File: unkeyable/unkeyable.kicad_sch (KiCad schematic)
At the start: 12 parts, among them SW1 1, SW10 F, SW11 J, SW12 K, SW2 C, SW3 3, SW4 Q, SW5 W, SW6 E, SW7 A, SW8 S, SW9 D

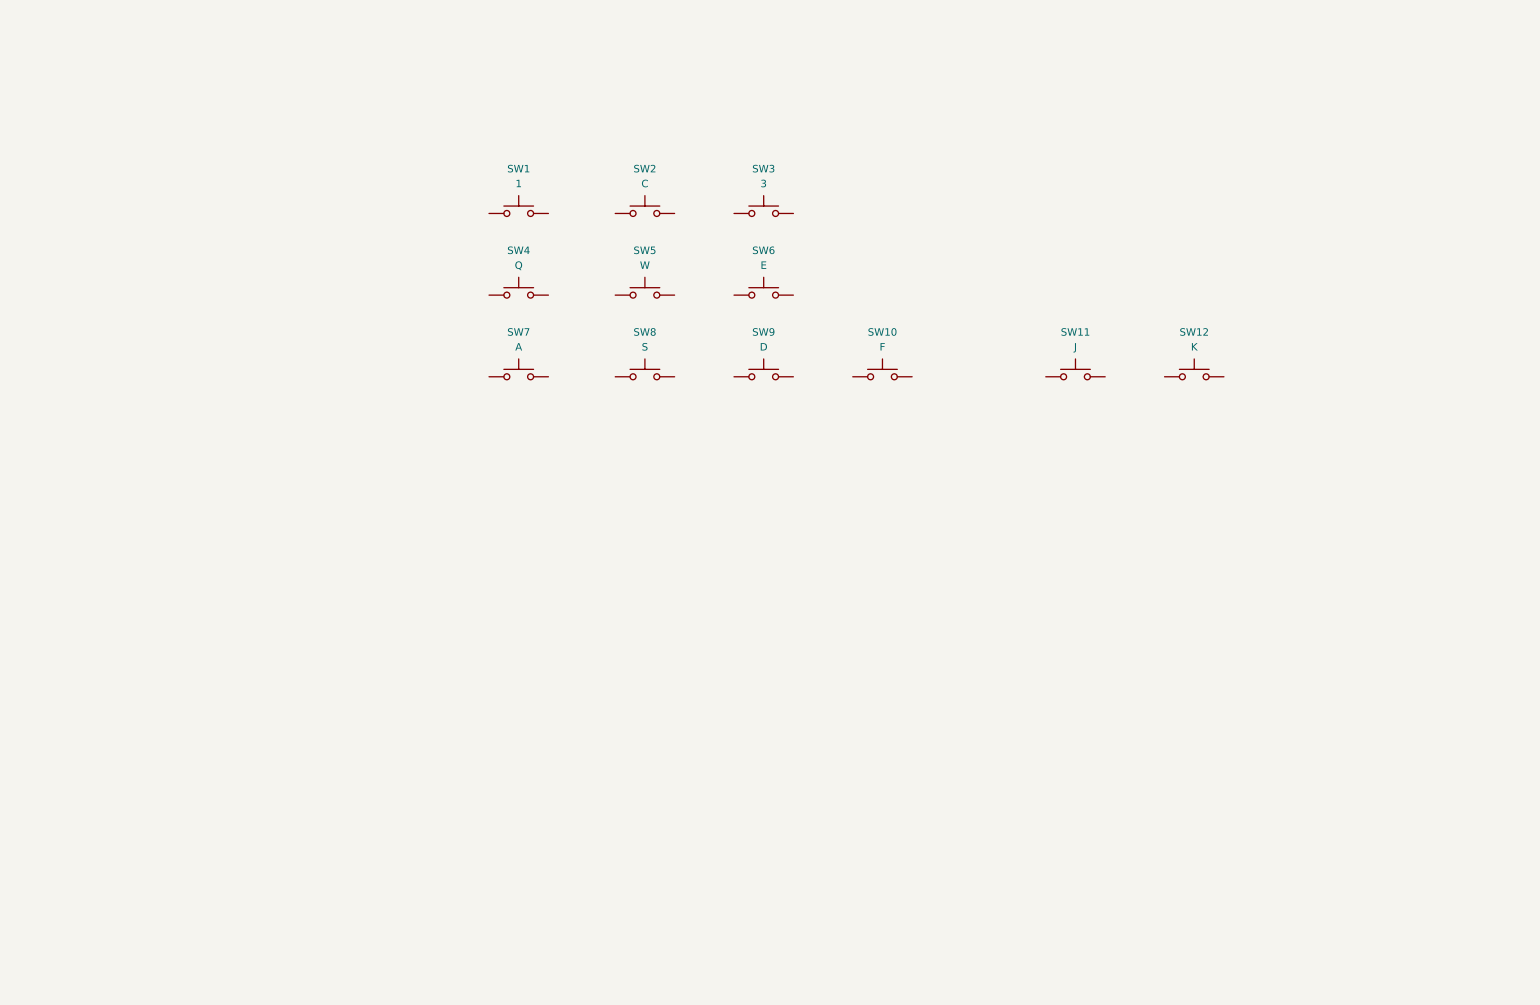
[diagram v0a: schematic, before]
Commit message: Adding RP2040 minimal viable schematic
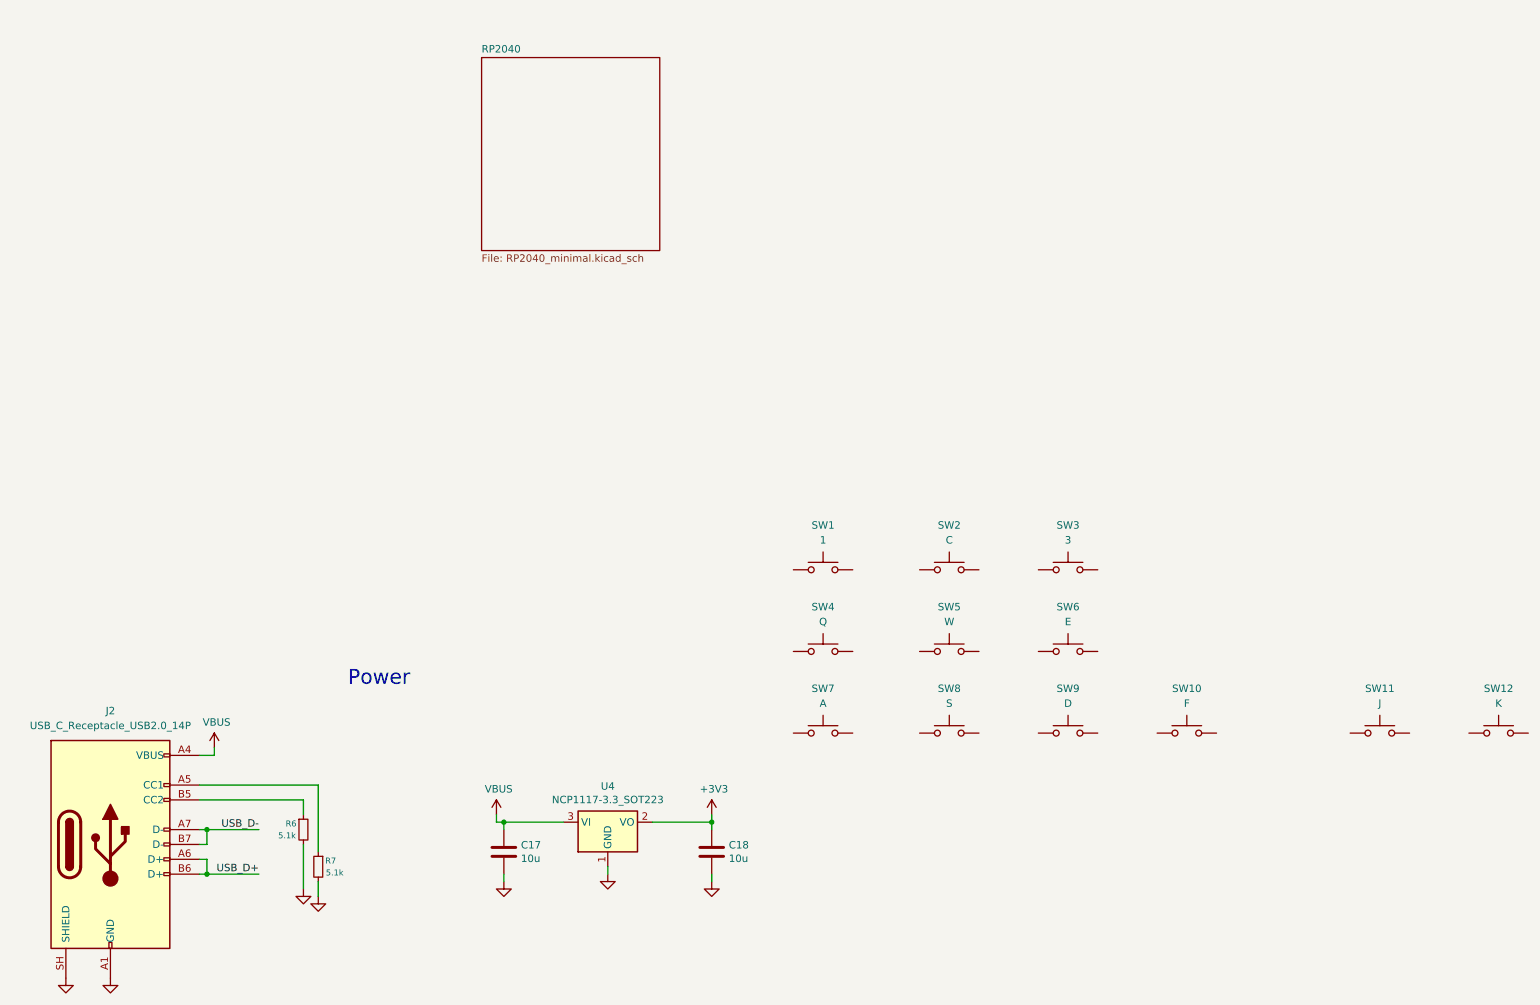
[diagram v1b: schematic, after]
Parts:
- added C17, C18: 10u, Capacitor_SMD:C_0805_2012Metric, symbol Device:C
- added J2: USB_C_Receptacle_USB2.0_14P, symbol Connector:USB_C_Receptacle_USB2.0_14P
- added R6, R7: 5.1k, symbol Device:R_Small
- added U4: NCP1117-3.3_SOT223, Package_TO_SOT_SMD:SOT-223-3_TabPin2, symbol Regulator_Linear:NCP1117-3.3_SOT223
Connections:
- new net: J2.A5 (CC1), R7.1
- new net: J2.B5 (CC2), R6.1
- new net +3V3: C18.1, U4.2 (VO)
- new net GND: C17.2, C18.2, J2.A1 (GND), J2.A12 (GND), J2.B1 (GND), J2.B12 (GND), J2.SH (SHIELD), R6.2, R7.2, U4.1 (GND)
- new net USB_D+: J2.A6 (D+), J2.B6 (D+)
- new net USB_D-: J2.A7 (D-), J2.B7 (D-)
- new net VBUS: C17.1, J2.A4 (VBUS), J2.A9 (VBUS), J2.B4 (VBUS), J2.B9 (VBUS), U4.3 (VI)
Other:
- added sheet RP2040 (RP2040_minimal.kicad_sch)
- note added: "Power"
- moved on the sheet: SW1, SW10, SW11, SW12, SW2, SW3, SW4, SW5, SW6, SW7, SW8, SW9

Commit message: working on Schematics
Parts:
- removed SW1: 1, Button_Switch_Keyboard:SW_Cherry_MX_1.00u_PCB, symbol Switch:SW_Push
- removed SW10: F, Button_Switch_Keyboard:SW_Cherry_MX_1.00u_PCB, symbol Switch:SW_Push
- removed SW11: J, Button_Switch_Keyboard:SW_Cherry_MX_1.00u_PCB, symbol Switch:SW_Push
- removed SW12: K, Button_Switch_Keyboard:SW_Cherry_MX_1.00u_PCB, symbol Switch:SW_Push
- removed SW2: C, Button_Switch_Keyboard:SW_Cherry_MX_1.00u_PCB, symbol Switch:SW_Push
- removed SW3: 3, Button_Switch_Keyboard:SW_Cherry_MX_1.00u_PCB, symbol Switch:SW_Push
- removed SW4: Q, Button_Switch_Keyboard:SW_Cherry_MX_1.00u_PCB, symbol Switch:SW_Push
- removed SW5: W, Button_Switch_Keyboard:SW_Cherry_MX_1.00u_PCB, symbol Switch:SW_Push
- removed SW6: E, Button_Switch_Keyboard:SW_Cherry_MX_1.00u_PCB, symbol Switch:SW_Push
- removed SW7: A, Button_Switch_Keyboard:SW_Cherry_MX_1.00u_PCB, symbol Switch:SW_Push
- removed SW8: S, Button_Switch_Keyboard:SW_Cherry_MX_1.00u_PCB, symbol Switch:SW_Push
- removed SW9: D, Button_Switch_Keyboard:SW_Cherry_MX_1.00u_PCB, symbol Switch:SW_Push
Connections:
- net VBUS renamed +5V
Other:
- added sheet Switch_Matrix (Switch_Matrix.kicad_sch)
- sheet RP2040 ports: added GPIO0, GPIO1, GPIO10, GPIO11, GPIO12, GPIO13, GPIO14, GPIO15, GPIO16, GPIO17, GPIO18, GPIO19, GPIO2, GPIO20, GPIO21, GPIO22, GPIO23, GPIO24, GPIO25, GPIO26_ADC0, GPIO27_ADC1, GPIO28_ADC2, GPIO29_ADC3, GPIO3, GPIO4, GPIO5, GPIO6, GPIO7, GPIO8, GPIO9, RUN, SWCLK, SWD, USB_D+, USB_D-; removed none
